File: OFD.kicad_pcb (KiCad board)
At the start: 2 copper layers, 68.8 x 200.4 mm, 115 parts, among them J1 Conn_01x02, J2 Conn_01x04, SW2 SW_TACT, U1 PMIC_HX3002, U2 MCU_CH552E

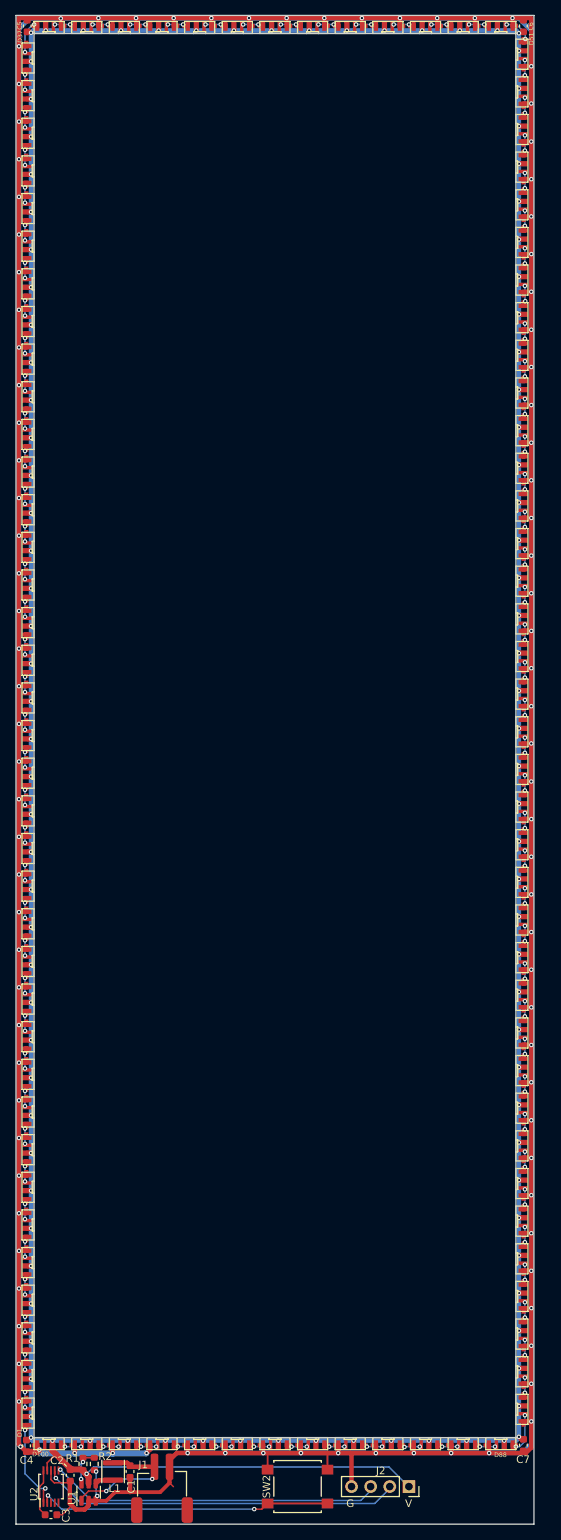
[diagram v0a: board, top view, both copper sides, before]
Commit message: PCB outline size modified
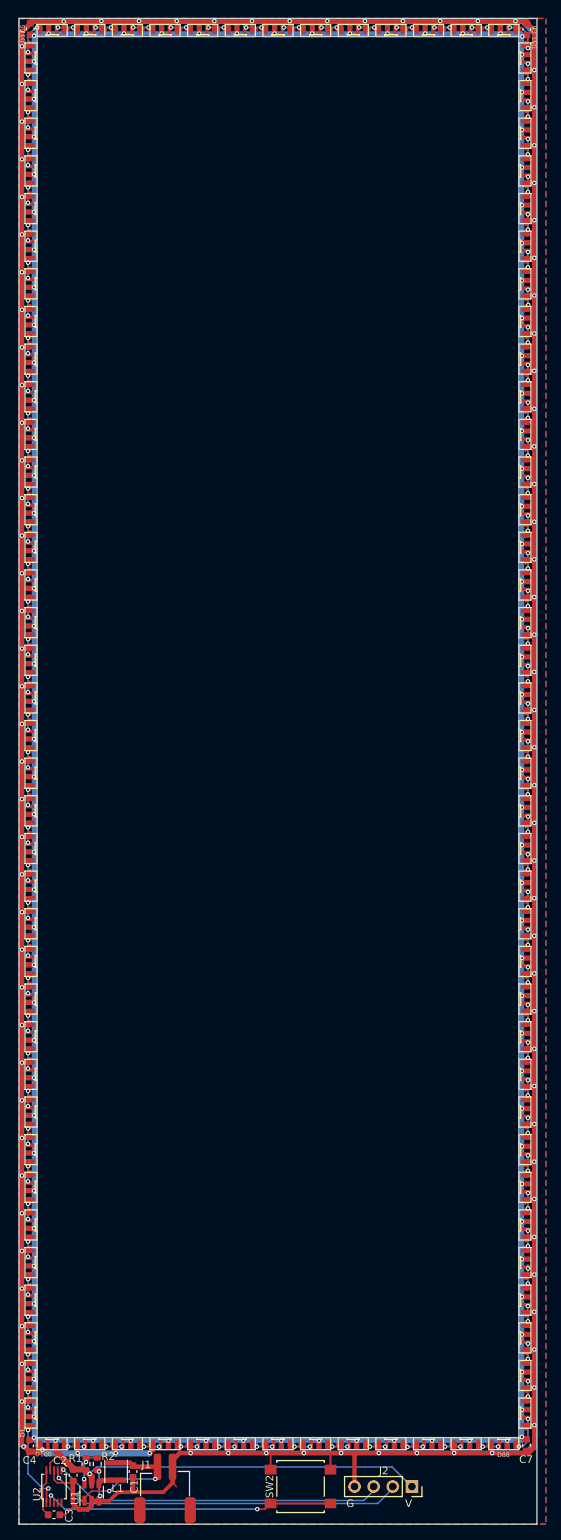
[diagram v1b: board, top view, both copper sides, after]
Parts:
- moved D51 0.64 mm to (67.3, 5.25)
- moved D52 0.64 mm to (67.3, 10.2)
- moved D53 0.64 mm to (67.3, 15.2)
- moved D54 0.64 mm to (67.3, 20.2)
- moved D55 0.64 mm to (67.3, 25.2)
- moved D56 0.64 mm to (67.3, 30.2)
- moved D57 0.64 mm to (67.3, 35.2)
- moved D58 0.64 mm to (67.3, 40.2)
- moved D59 0.64 mm to (67.3, 45.2)
- moved D60 0.64 mm to (67.3, 50.2)
- moved D61 0.64 mm to (67.3, 55.2)
- moved D62 0.64 mm to (67.3, 60.2)
- moved D63 0.64 mm to (67.3, 65.2)
- moved D64 0.64 mm to (67.3, 70.2)
- moved D65 0.64 mm to (67.3, 75.2)
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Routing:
- net GND: track 1158.5 -> 1155.8 mm
- net Net-(D50-Pad3): track 4.05 -> 5.19 mm
- net +5V: track 583.5 -> 582.6 mm
- net Net-(D83-Pad3): track 2.36 -> 2.86 mm
- added copper zone on B.Cu, net GND
- added copper zone on F.Cu, net GND
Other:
- board size 68.8 x 200.4 mm -> 68.8 x 200 mm

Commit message: fixed D66's unconnection
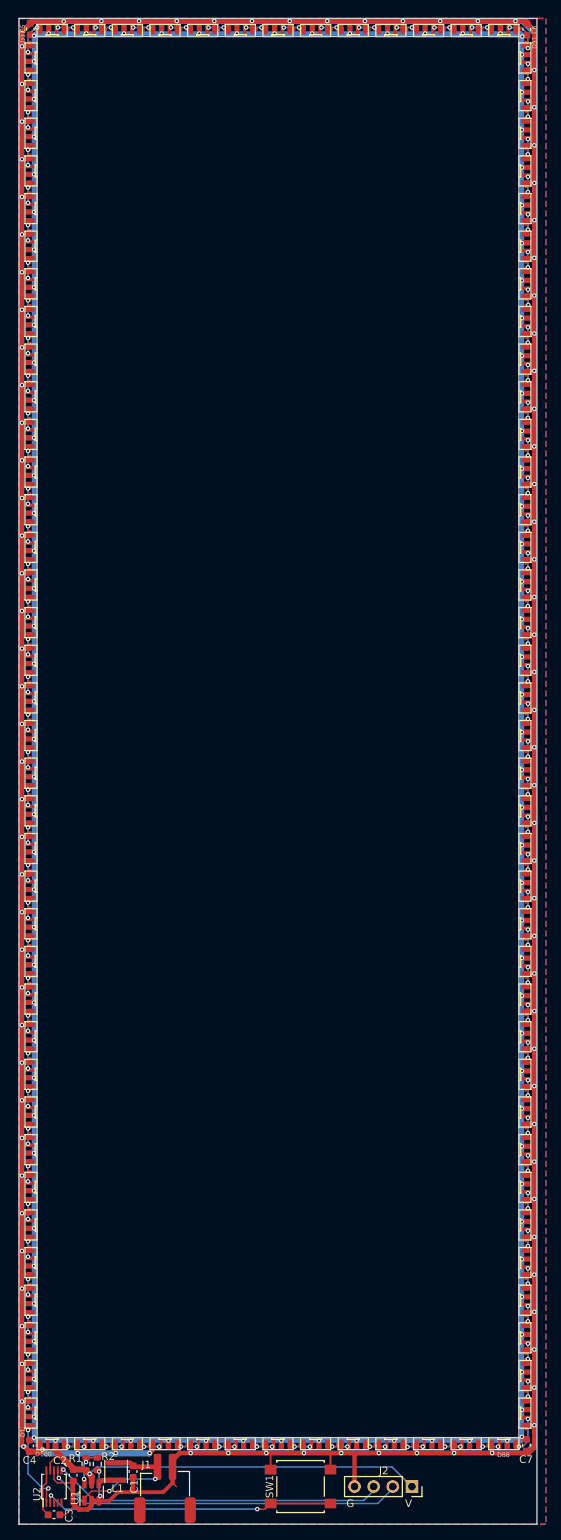
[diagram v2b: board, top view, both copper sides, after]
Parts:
- renumbered SW2 to SW1
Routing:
- net Net-(D83-Pad3): track 2.86 -> 2.36 mm
